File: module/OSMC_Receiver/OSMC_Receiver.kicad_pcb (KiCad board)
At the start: 4 copper layers, 120.1 x 78.2 mm, 91 parts, among them U1 24AA02-OT, U13 OSMC Module Board, U14 OSMC Module Board, U15 OSMC Module Board, U16 OSMC Module Board, U17 OSMC Module Board, U18 OSMC Module Board, U19 OSMC Module Board, U2 LTC4317, U20 OSMC Module Board, U3 XIAO-ESP32-S3-DIP, U4 PCF8574DWR, U5 LTC4317, U6 LTC4317, U7 LTC4317

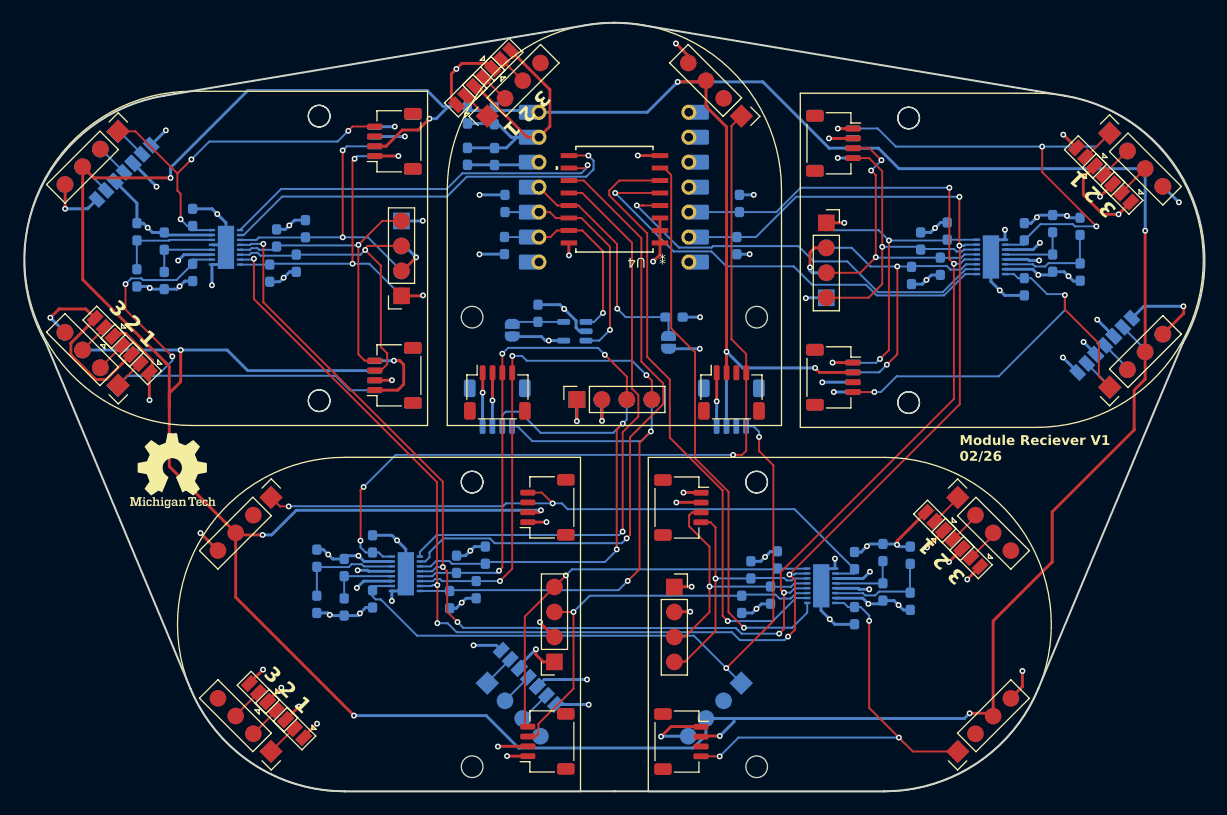
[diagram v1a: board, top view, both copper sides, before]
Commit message: update to modules gerbers produced
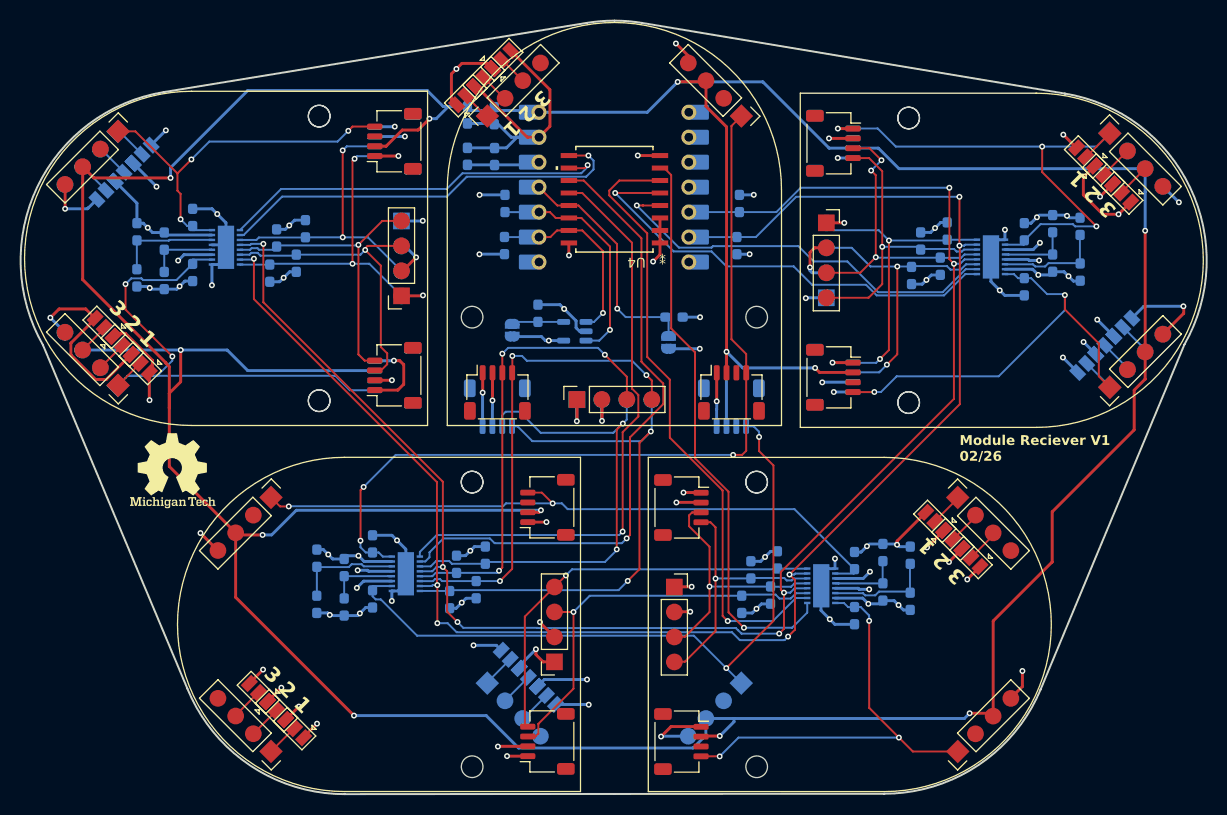
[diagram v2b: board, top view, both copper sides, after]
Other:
- board size 120.1 x 78.2 mm -> 120.7 x 78.7 mm
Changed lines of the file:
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@@
 	)
 	(gr_line
-		(start 158.201092 56.262356)
-		(end 201.241007 63.452348)
+		(start 158.2 56.04)
+		(end 201.239915 63.229992)
 		(stroke
 			(width 0.2)
@@
 	)
 	(gr_arc
-		(start 155.4 56.03)
-		(mid 156.805356 56.088187)
-		(end 158.201092 56.262356)
+		(start 155.4 55.81)
+		(mid 156.805356 55.868187)
+		(end 158.201092 56.042356)
 		(stroke
 			(width 0.2)
@@
 	)
 	(gr_line
-		(start 152.598902 56.262357)
-		(end 109.559061 63.452358)
+		(start 152.6 56.04)
+		(end 109.559061 63.08)
 		(stroke
 			(width 0.2)
@@
 	)
 	(gr_arc
-		(start 201.24101 63.452348)
-		(mid 213.795909 72.926513)
-		(end 213.206132 88.64395)
+		(start 201.229915 63.229992)
+		(mid 213.982216 72.811701)
+		(end 213.395121 88.751766)
 		(stroke
 			(width 0.2)
@@
 	)
 	(gr_line
-		(start 112.275211 123.765527)
-		(end 97.593633 88.643383)
+		(start 111.96 123.765527)
+		(end 97.274524 88.825419)
 		(stroke
 			(width 0.2)
@@
 	)
 	(gr_arc
-		(start 127.960001 134.209053)
-		(mid 118.53822 131.359318)
-		(end 112.27521 123.765527)
+		(start 127.960001 134.500271)
+		(mid 118.326274 131.567948)
+		(end 111.96 123.765527)
 		(stroke
 			(width 0.2)
@@
 	)
 	(gr_line
-		(start 155.4 134.209053)
-		(end 182.853008 134.209053)
+		(start 155.4 134.48)
+		(end 182.853008 134.46)
 		(stroke
 			(width 0.2)
@@
 	)
 	(gr_arc
-		(start 97.593632 88.643383)
-		(mid 97.004212 72.926253)
-		(end 109.558928 63.452358)
+		(start 97.274523 88.825419)
+		(mid 96.685574 72.74088)
+		(end 109.559061 63.08)
 		(stroke
 			(width 0.2)
@@
 	)
 	(gr_line
-		(start 155.4 134.209053)
-		(end 127.960001 134.209053)
+		(start 155.4 134.48)
+		(end 127.960001 134.500271)
 		(stroke
 			(width 0.2)
@@
 	)
 	(gr_arc
-		(start 152.598902 56.262357)
-		(mid 153.994641 56.088188)
-		(end 155.4 56.03)
+		(start 152.6 56.04)
+		(mid 153.995318 55.86821)
+		(end 155.4 55.810819)
 		(stroke
 			(width 0.2)
@@
 	)
 	(gr_arc
-		(start 198.524799 123.765508)
-		(mid 192.267199 131.355702)
-		(end 182.853008 134.209053)
+		(start 198.756365 123.862307)
+		(mid 192.406295 131.564597)
+		(end 182.853008 134.46)
 		(stroke
 			(width 0.2)
@@
 	)
 	(gr_line
-		(start 198.524799 123.765508)
-		(end 213.206132 88.64395)
+		(start 198.756365 123.862307)
+		(end 213.395119 88.751766)
 		(stroke
 			(width 0.2)

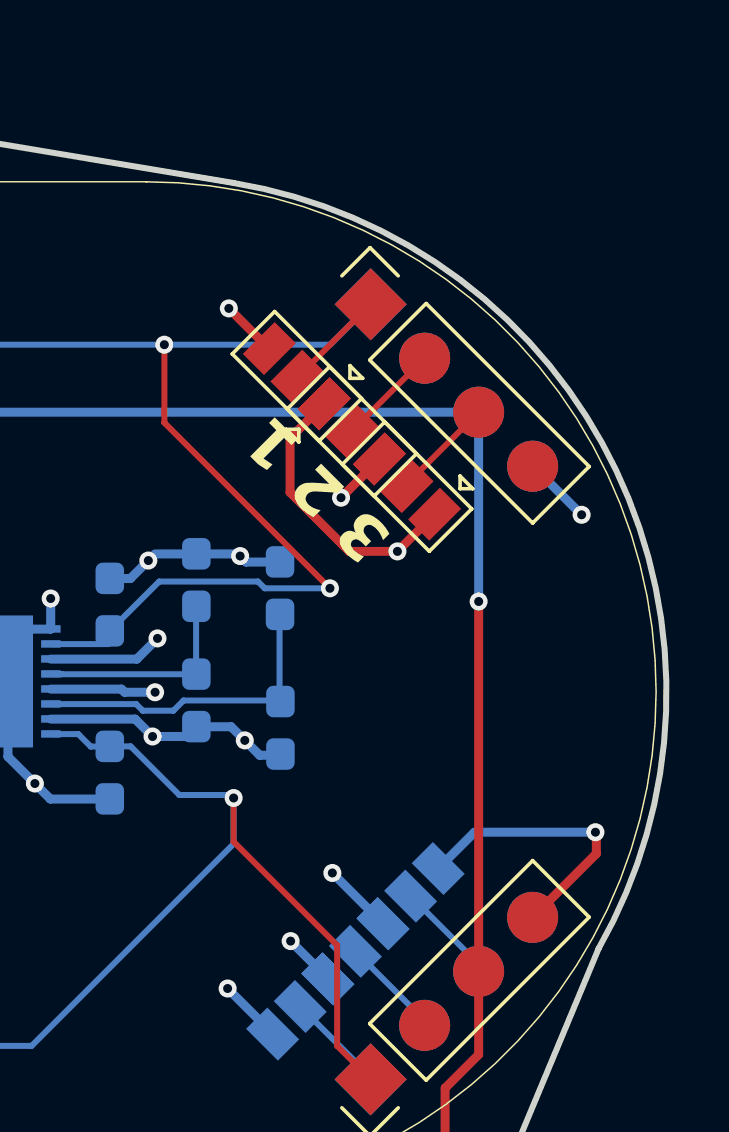
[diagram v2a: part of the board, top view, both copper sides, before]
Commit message: fixed diode direction
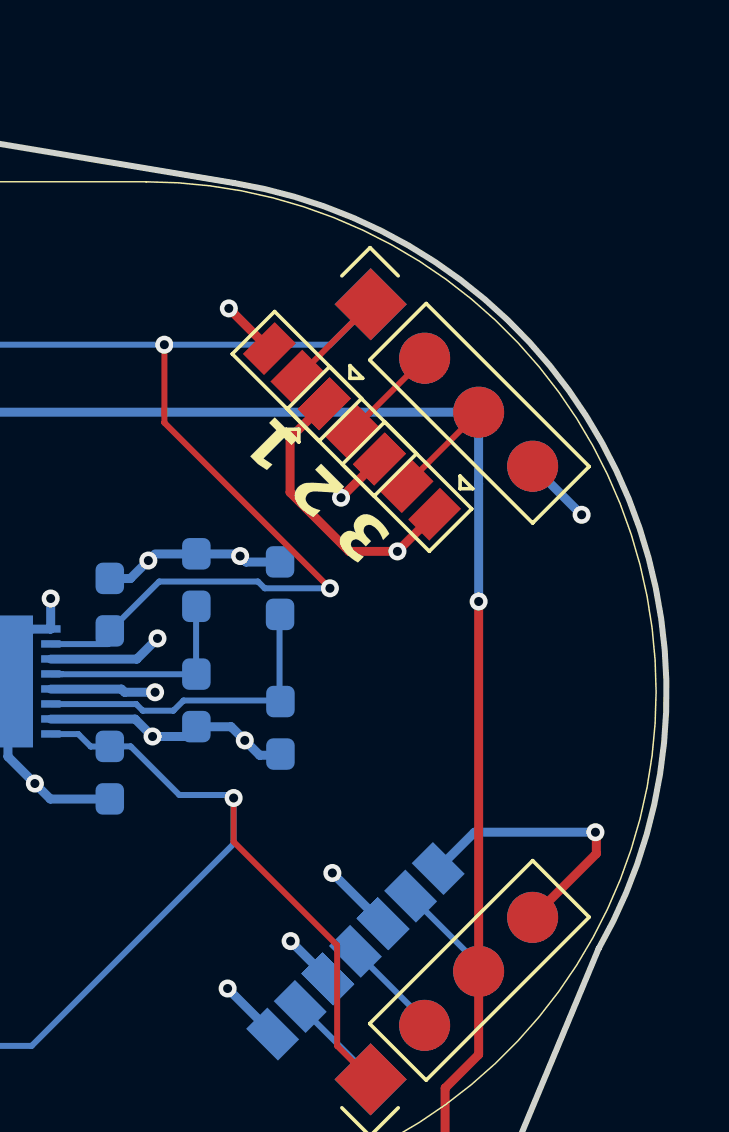
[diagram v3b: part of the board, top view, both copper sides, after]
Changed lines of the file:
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@@
 	)
 	(gr_arc
-		(start 201.229915 63.229992)
-		(mid 213.982216 72.811701)
-		(end 213.395121 88.751766)
+		(start 201.239915 63.229992)
+		(mid 213.985804 72.815458)
+		(end 213.39653 88.752571)
 		(stroke
 			(width 0.2)

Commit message: created all gerber zips
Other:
- board text added: "Module Reciever V1.1 02/26"
- board text removed: "Module Reciever V1 02/26"
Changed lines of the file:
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@@
 		)
 	)
-	(gr_text "Module Reciever V1\n02/26"
+	(gr_text "Module Reciever V1.1\n02/26"
 		(at 190.51 100.71 0)
 		(layer "F.SilkS")

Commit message: board update
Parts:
- R12: value 182k -> 1M
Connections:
- U17 pad 3: /Modules/SCL4 -> /Modules/SDA4
- U17 pad 4: /Modules/SDA4 -> /Modules/SCL4
- U17 pad 7: /Modules/SCL4 -> /Modules/SDA4
- U17 pad 8: /Modules/SDA4 -> /Modules/SCL4
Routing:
- net /Modules/SDA4: track 30.9 -> 31.5 mm
- net /Modules/SCL4: track 31.2 -> 30.7 mm
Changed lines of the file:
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@@
 			(layers "F.Cu" "F.Mask" "F.Paste")
 			(roundrect_rratio 0.25)
-			(net 37 "/Modules/SCL4")
+			(net 38 "/Modules/SDA4")
 			(pinfunction "SDA")
 			(pintype "bidirectional")
@@
 			(layers "F.Cu" "F.Mask" "F.Paste")
 			(roundrect_rratio 0.25)
-			(net 38 "/Modules/SDA4")
+			(net 37 "/Modules/SCL4")
 			(pinfunction "SCL")
 			(pintype "input")
@@
 			(size 1.7 1.7)
 			(layers "F.Cu" "F.Mask" "F.Paste")
-			(net 37 "/Modules/SCL4")
+			(net 38 "/Modules/SDA4")
 			(pinfunction "SDA")
 			(pintype "bidirectional")
@@
 			(size 1.7 1.7)
 			(layers "F.Cu" "F.Mask" "F.Paste")
-			(net 38 "/Modules/SDA4")
+			(net 37 "/Modules/SCL4")
 			(pinfunction "SCL")
 			(pintype "input")
@@
 			)
 		)
-		(property "Value" "182k"
+		(property "Value" "1M"
 			(at 0 -1.43 90)
 			(layer "B.Fab")
@@
 	)
 	(segment
-		(start 130.05 78.965)
-		(end 130.29 78.725)
-		(width 0.2)
-		(layer "F.Cu")
-		(net 37)
-	)
-	(segment
-		(start 131.655 91.395)
-		(end 131.03 91.395)
-		(width 0.2)
-		(layer "F.Cu")
-		(net 37)
-	)
-	(segment
-		(start 130.29 78.725)
-		(end 133.745 78.725)
-		(width 0.2)
-		(layer "F.Cu")
-		(net 37)
-	)
-	(segment
-		(start 131.64 80.73)
-		(end 131.64 89.01)
+		(start 129.575 78.515057)
+		(end 131.905057 76.185)
 		(width 0.2)
 		(layer "F.Cu")
@@
 	)
 	(segment
-		(start 130.05 79.14)
-		(end 131.64 80.73)
+		(start 129.575 89.845)
+		(end 130.125 90.395)
 		(width 0.2)
 		(layer "F.Cu")
@@
 	)
 	(segment
-		(start 132.29 89.66)
-		(end 132.29 90.76)
+		(start 129.575 79.615)
+		(end 129.575 89.845)
 		(width 0.2)
 		(layer "F.Cu")
@@
 	)
 	(segment
-		(start 132.29 90.76)
-		(end 131.655 91.395)
+		(start 129.575 79.615)
+		(end 129.575 78.515057)
 		(width 0.2)
 		(layer "F.Cu")
@@
 	)
 	(segment
-		(start 131.64 89.01)
-		(end 132.29 89.66)
+		(start 131.905057 76.185)
+		(end 133.745 76.185)
 		(width 0.2)
 		(layer "F.Cu")
@@
 	)
 	(segment
-		(start 130.05 79.14)
-		(end 130.05 78.965)
+		(start 130.125 90.395)
+		(end 131.03 90.395)
 		(width 0.2)
 		(layer "F.Cu")
@@
 	)
 	(via
-		(at 130.05 79.14)
+		(at 129.575 79.615)
 		(size 0.6)
 		(drill 0.3)
@@
 	)
 	(segment
-		(start 129.575 79.615)
-		(end 123.04 79.615)
-		(width 0.2)
-		(layer "B.Cu")
-		(net 37)
-	)
-	(segment
 		(start 118.290057 79.62)
 		(end 118.481057 79.429)
@@
 	)
 	(segment
-		(start 130.05 79.14)
-		(end 129.575 79.615)
+		(start 129.575 79.615)
+		(end 123.04 79.615)
 		(width 0.2)
 		(layer "B.Cu")
@@
 	)
 	(segment
-		(start 131.795 76.185)
-		(end 129.36 78.62)
+		(start 131.995 91.395)
+		(end 132.369 91.021)
 		(width 0.2)
 		(layer "F.Cu")
@@
 	)
 	(segment
-		(start 129.36 89.76)
-		(end 129.995 90.395)
+		(start 133.7 78.68)
+		(end 133.745 78.725)
 		(width 0.2)
 		(layer "F.Cu")
@@
 	)
 	(segment
-		(start 133.745 76.185)
-		(end 131.795 76.185)
+		(start 130.26 78.68)
+		(end 133.7 78.68)
 		(width 0.2)
 		(layer "F.Cu")
@@
 	)
 	(segment
-		(start 129.36 78.62)
-		(end 129.36 89.76)
+		(start 131.03 91.395)
+		(end 131.995 91.395)
 		(width 0.2)
 		(layer "F.Cu")
@@
 	)
 	(segment
-		(start 129.995 90.395)
-		(end 131.03 90.395)
+		(start 132.369 91.021)
+		(end 132.369 80.789)
+		(width 0.2)
+		(layer "F.Cu")
+		(net 38)
+	)
+	(segment
+		(start 132.369 80.789)
+		(end 130.26 78.68)
 		(width 0.2)
 		(layer "F.Cu")
@@
 	)
 	(via
-		(at 129.36 78.62)
+		(at 130.26 78.68)
 		(size 0.6)
 		(drill 0.3)
@@
 	)
 	(segment
+		(start 130.26 78.68)
+		(end 129.3 78.68)
+		(width 0.2)
+		(layer "B.Cu")
+		(net 38)
+	)
+	(segment
 		(start 119.093862 78.96)
 		(end 119.253862 79.12)
@@
 	)
 	(segment
-		(start 119.253862 79.12)
-		(end 120.715 79.12)
+		(start 121.154 78.681)
+		(end 121.04 78.795)
 		(width 0.2)
 		(layer "B.Cu")
@@
 	)
 	(segment
-		(start 129.36 78.62)
-		(end 129.299 78.681)
+		(start 119.253862 79.12)
+		(end 120.715 79.12)
 		(width 0.2)
 		(layer "B.Cu")
@@
 	)
 	(segment
-		(start 129.299 78.681)
-		(end 121.154 78.681)
+		(start 129.3 78.68)
+		(end 129.299 78.681)
 		(width 0.2)
 		(layer "B.Cu")
@@
 	)
 	(segment
-		(start 121.154 78.681)
-		(end 121.04 78.795)
+		(start 129.299 78.681)
+		(end 121.154 78.681)
 		(width 0.2)
 		(layer "B.Cu")
